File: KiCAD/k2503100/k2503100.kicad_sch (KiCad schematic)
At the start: 0 parts

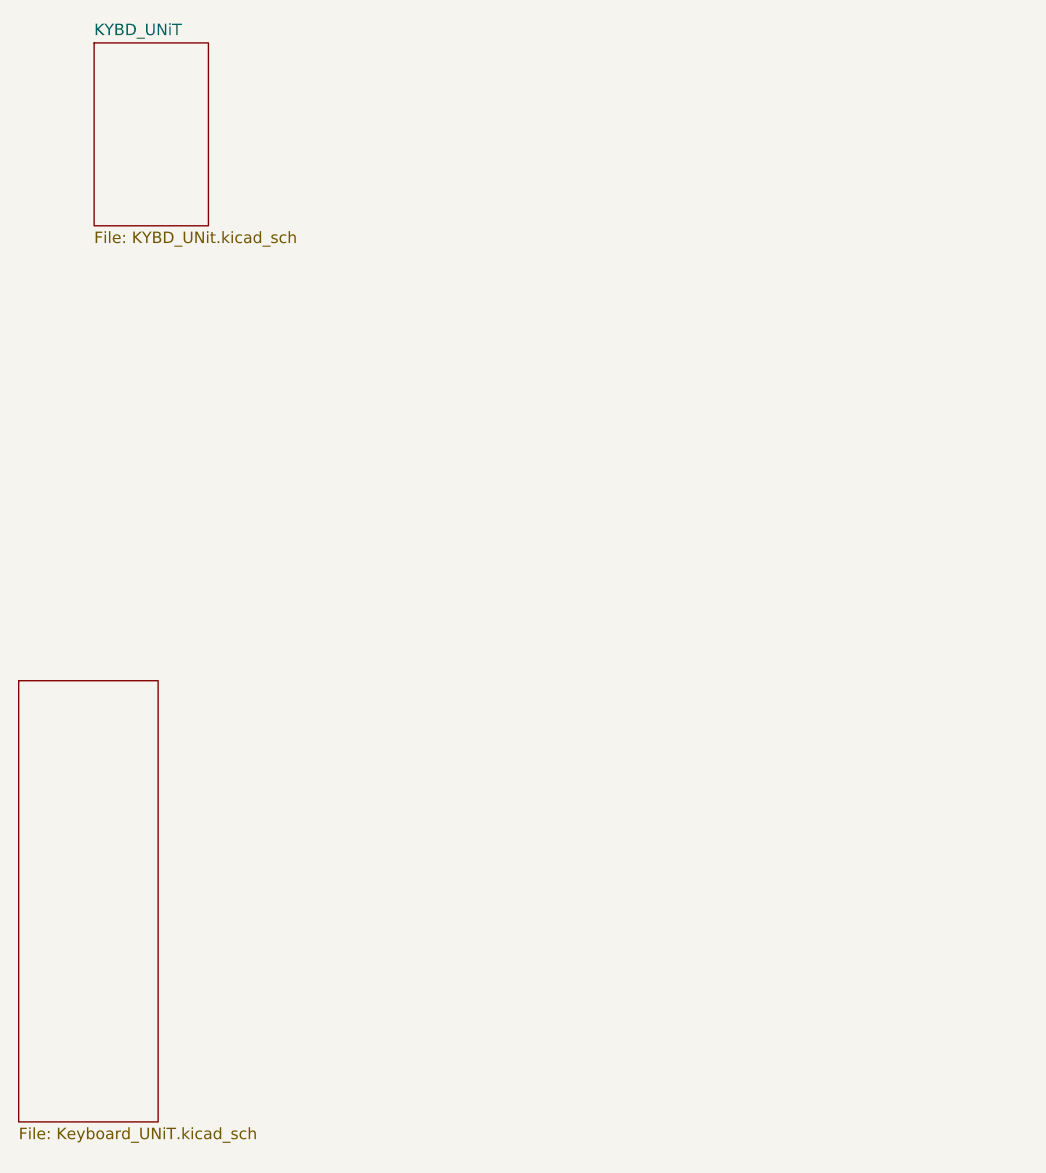
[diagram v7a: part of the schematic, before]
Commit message: 未使用回路の削除
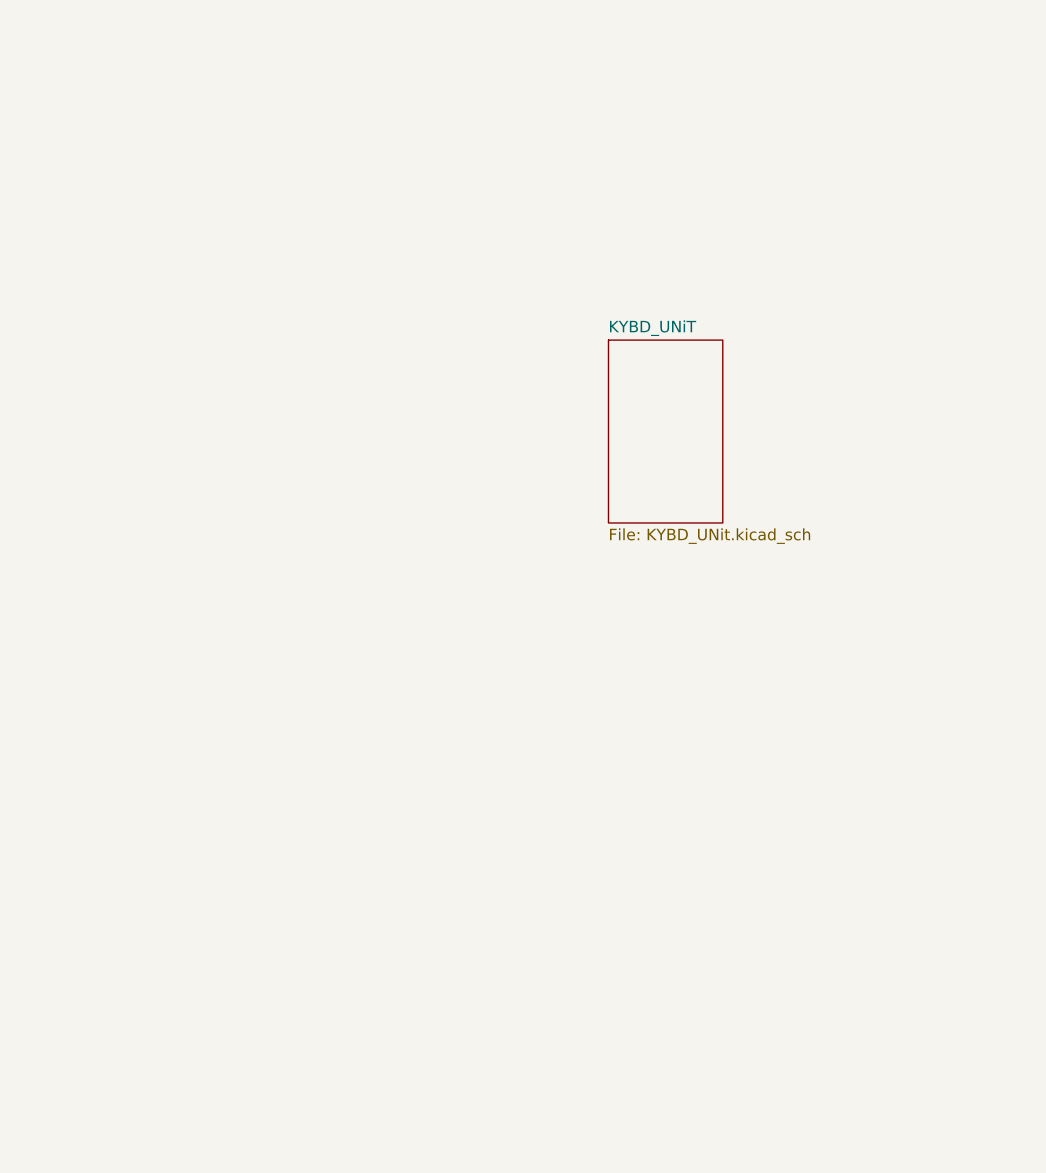
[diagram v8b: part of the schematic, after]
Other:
- removed sheet Keyboard_UNiT
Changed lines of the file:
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@@
 	)
 	(sheet
-		(at 29.718 128.016)
-		(size 15.494 49.022)
-		(fields_autoplaced yes)
-		(stroke
-			(width 0.1524)
-			(type solid)
-		)
-		(fill
-			(color 0 0 0 0.0000)
-		)
-		(property "Sheetname" "Keyboard_UNiT"
-			(at 29.718 127.3044 0)
-			(effects
-				(font
-					(size 1.27 1.27)
-				)
-				(justify left bottom)
-				(hide yes)
-			)
-		)
-		(property "Sheetfile" "Keyboard_UNiT.kicad_sch"
-			(at 29.718 177.6226 0)
-			(effects
-				(font
-					(size 1.27 1.27)
-				)
-				(justify left top)
-			)
-		)
-		(instances
-			(project "k2503100"
-				(path "/e63e39d7-6ac0-4ffd-8aa3-1841a4541b55"
-					(page "2")
-				)
-			)
-		)
-	)
-	(sheet
-		(at 38.1 57.15)
+		(at 95.25 90.17)
 		(size 12.7 20.32)
 		(fields_autoplaced yes)
@@
 		)
 		(property "Sheetname" "KYBD_UNiT"
-			(at 38.1 56.4384 0)
+			(at 95.25 89.4584 0)
 			(effects
 				(font
@@
 		)
 		(property "Sheetfile" "KYBD_UNit.kicad_sch"
-			(at 38.1 78.0546 0)
+			(at 95.25 111.0746 0)
 			(effects
 				(font
